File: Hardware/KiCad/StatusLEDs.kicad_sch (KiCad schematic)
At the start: 18 parts

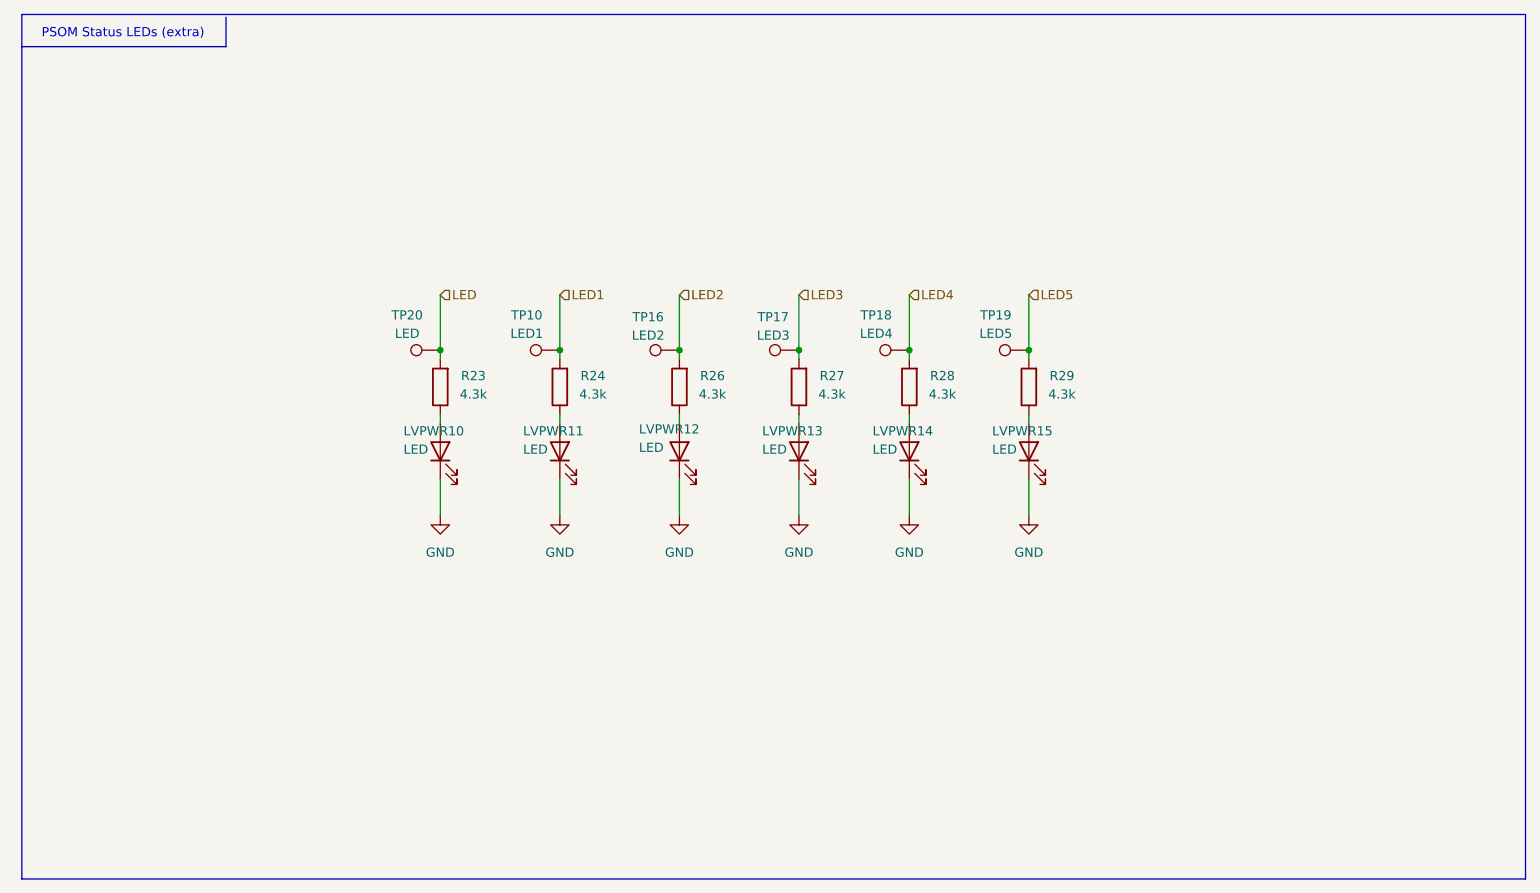
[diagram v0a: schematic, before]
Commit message: schematic changes, pre pcb revB changes
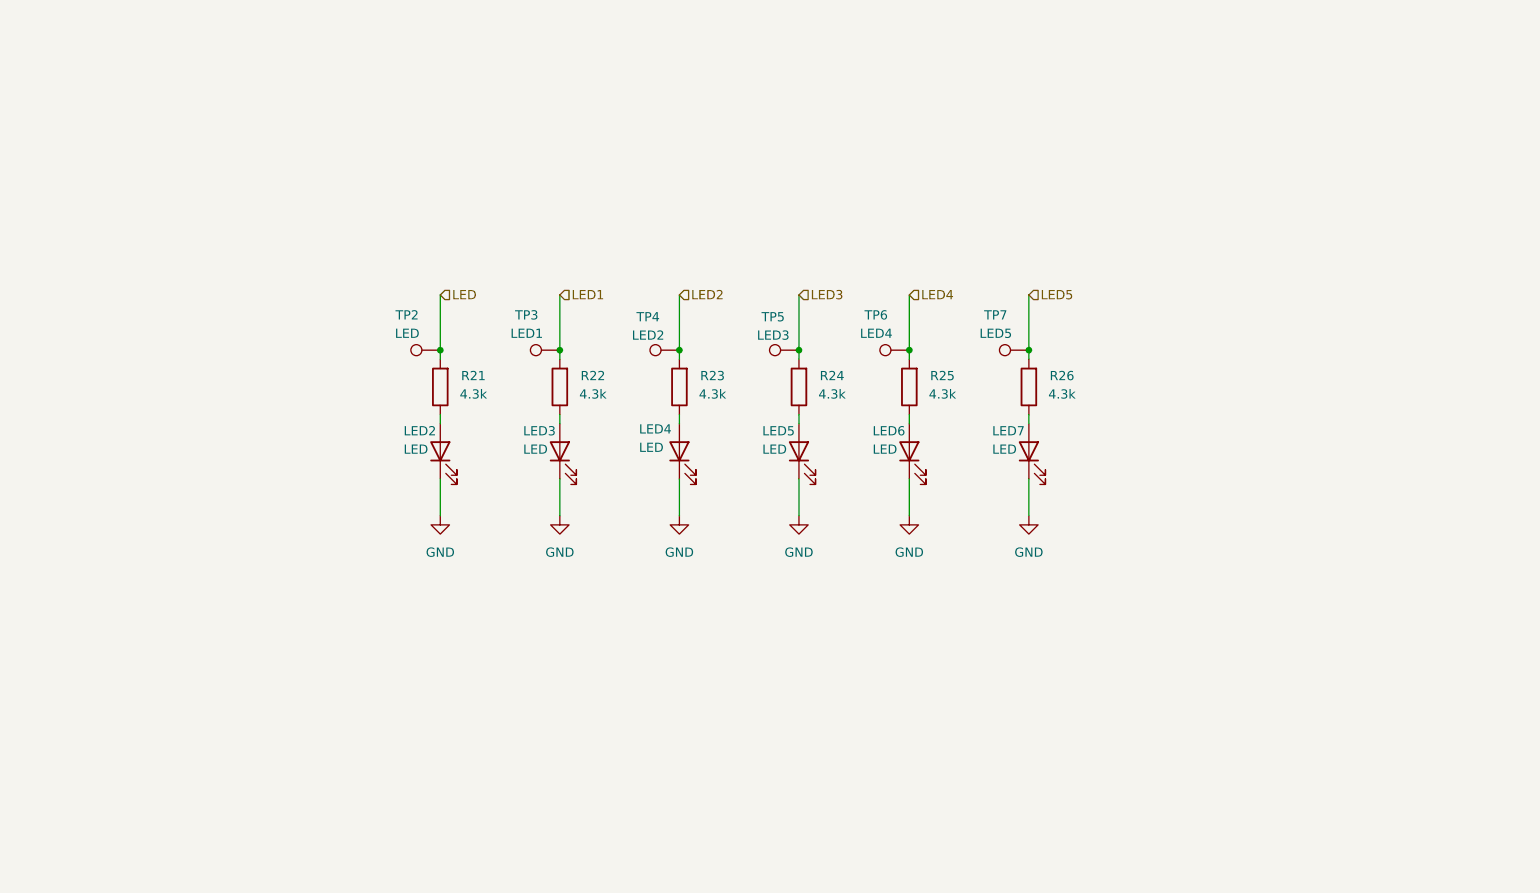
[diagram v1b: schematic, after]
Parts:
- R21: renamed from R23; LCSC (none) -> C2907165
- R22: renamed from R24; LCSC (none) -> C2907165
- R23: renamed from R26; LCSC (none) -> C2907165
- R24: renamed from R27; LCSC (none) -> C2907165
- R25: renamed from R28; LCSC (none) -> C2907165
- R26: renamed from R29; LCSC (none) -> C2907165
- renumbered LVPWR10 to LED2, LVPWR11 to LED3, LVPWR12 to LED4, LVPWR13 to LED5, LVPWR14 to LED6, LVPWR15 to LED7, TP20 to TP2, TP10 to TP3, TP16 to TP4, TP17 to TP5, TP18 to TP6, TP19 to TP7
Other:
- note removed: "PSOM Status LEDs (extra)"

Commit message: sch changes, pre pcb changes
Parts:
- removed LED2, LED3, LED4, LED5, LED6, LED7: LED, LED_SMD:LED_0603_1608Metric, symbol Device:LED
- removed R21, R22, R23, R24, R25, R26: 4.3k, Resistor_SMD:R_0603_1608Metric_Pad0.98x0.95mm_HandSolder, symbol Device:R
- removed TP2: LED, TestPoint:TestPoint_Pad_1.0x1.0mm, symbol Connector:TestPoint
- removed TP3: LED1, TestPoint:TestPoint_Pad_1.0x1.0mm, symbol Connector:TestPoint
- removed TP4: LED2, TestPoint:TestPoint_Pad_1.0x1.0mm, symbol Connector:TestPoint
- removed TP5: LED3, TestPoint:TestPoint_Pad_1.0x1.0mm, symbol Connector:TestPoint
- removed TP6: LED4, TestPoint:TestPoint_Pad_1.0x1.0mm, symbol Connector:TestPoint
- removed TP7: LED5, TestPoint:TestPoint_Pad_1.0x1.0mm, symbol Connector:TestPoint
